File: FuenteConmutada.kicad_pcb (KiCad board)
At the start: 2 copper layers, 50 x 50 mm, 25 parts, among them J1 Conn_01x02_Socket, J2 Conn_01x03_Socket, U1 MT3608

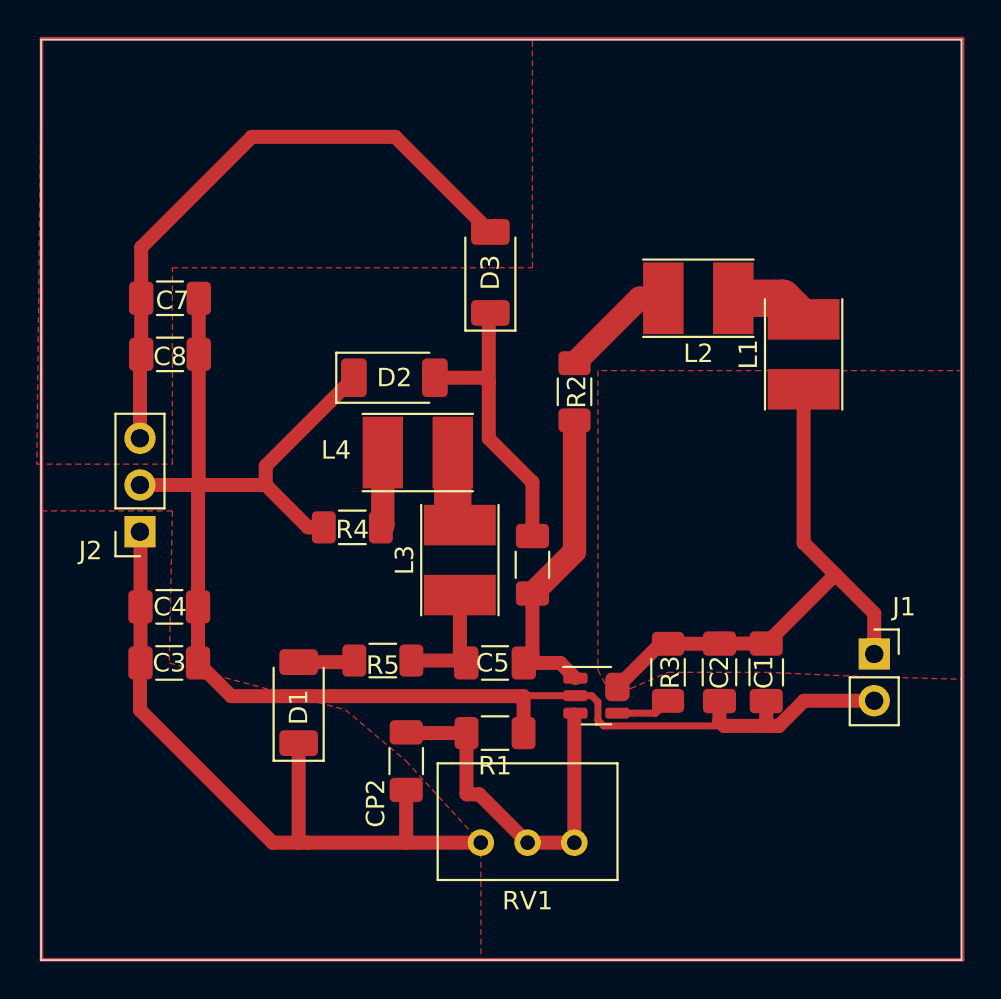
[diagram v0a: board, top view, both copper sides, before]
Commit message: Ajustes planos y tracks
Agrandar Margen a 40mils de los planos
Cambiar Rmed de lado del inductor (hacia Vin)
Cambiar Pos Inductores, mas cerca de SW
Aumentar a 50mils todos los tracks que no esten embutidos en planos
Puente en GND/Vfedback para no pasar debajo del SOT23
-Verificar cambios y poner Listo en la wiki
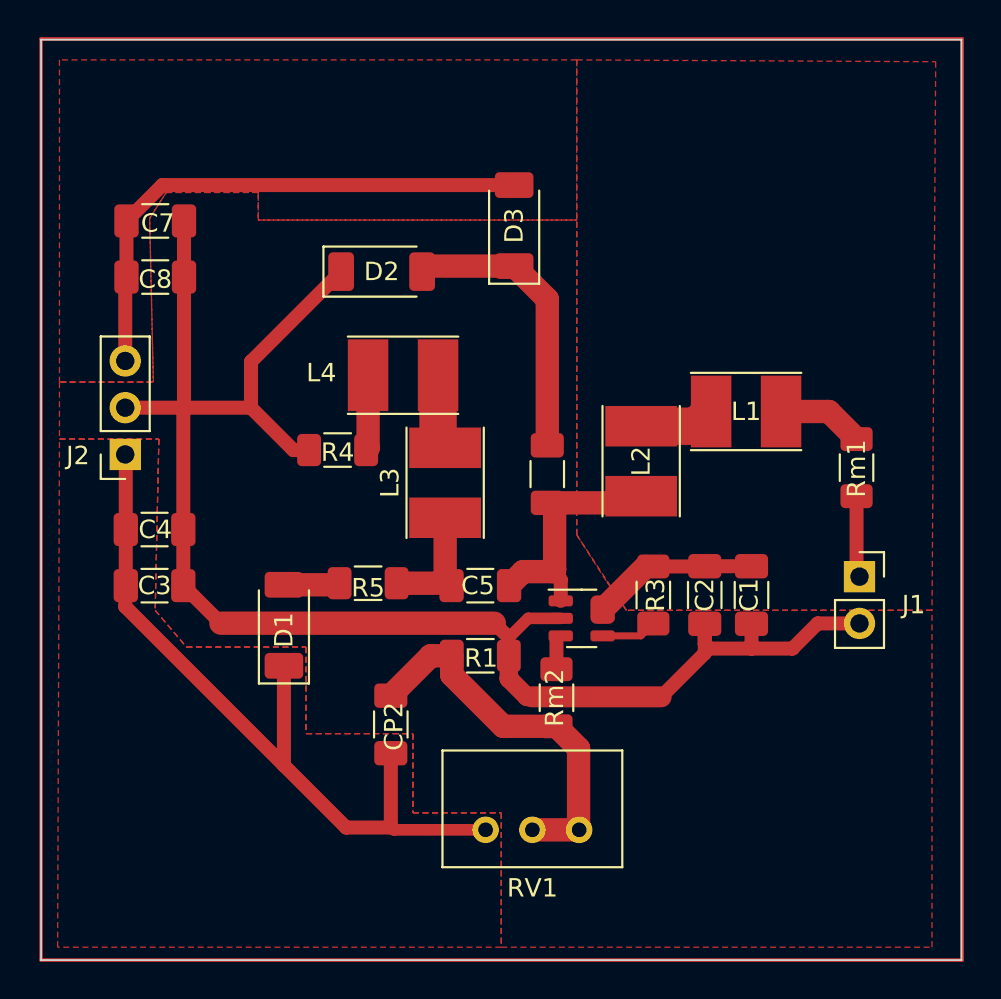
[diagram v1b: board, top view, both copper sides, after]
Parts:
- removed R2: R, Resistor_SMD:R_1206_3216Metric_Pad1.30x1.75mm_HandSolder
- added Rm1: R, Resistor_SMD:R_1206_3216Metric_Pad1.30x1.75mm_HandSolder, F.Cu at (109.3, 99.2)
- added Rm2: R, Resistor_SMD:R_1206_3216Metric_Pad1.30x1.75mm_HandSolder, F.Cu at (93.0, 111.8)
- moved L2 9.38 mm to (97.6, 98.9), turned to -90 degrees
- moved D2 5.81 mm to (83.5, 88.6)
- moved CP1 4.99 mm to (92.5, 99.6)
- moved L1 4.41 mm to (103.3, 96.2), turned to 180 degrees
- moved C3 4.28 mm to (71.2, 105.7)
- moved C4 4.28 mm to (71.2, 102.6)
- moved C5 4.28 mm to (88.9, 105.7)
- moved C7 4.28 mm to (71.2, 85.8)
- moved C8 4.28 mm to (71.2, 88.9)
- moved J2 4.28 mm to (69.6, 98.5)
- moved R1 4.28 mm to (88.9, 109.5)
- moved D1 4.28 mm to (78.2, 107.8)
- moved J1 4.28 mm to (109.5, 105.2)
- moved L3 4.28 mm to (87.0, 100.1)
- moved L4 4.28 mm to (84.7, 94.2)
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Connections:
- CP2 pad 1: Net-(U1-FB) -> Net-(CP2-Pad1)
- L1 pad 1: /Vin -> Net-(L1-Pad1)
- L2 pad 2: Net-(L2-Pad2) -> Net-(U1-SW)
- R1 pad 1: Net-(U1-FB) -> Net-(CP2-Pad1)
- RV1 pad 2: Net-(U1-FB) -> Net-(CP2-Pad1)
- RV1 pad 3: Net-(U1-FB) -> Net-(CP2-Pad1)
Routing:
- net Net-(CP2-Pad1): track 0.00 -> 20.8 mm
- net Net-(U1-FB): track 20.6 -> 2.23 mm
- net /Vin: track 30.8 -> 14.0 mm
- net GND: track 82.8 -> 89.8 mm
- net Net-(L2-Pad2): track 6.29 -> 0.00 mm
- net Net-(L1-Pad1): track 0.00 -> 4.72 mm
- net /Vo-: track 34.0 -> 29.5 mm
- net Net-(U1-SW): track 17.5 -> 13.7 mm
- net /Vo+: track 39.5 -> 42.4 mm

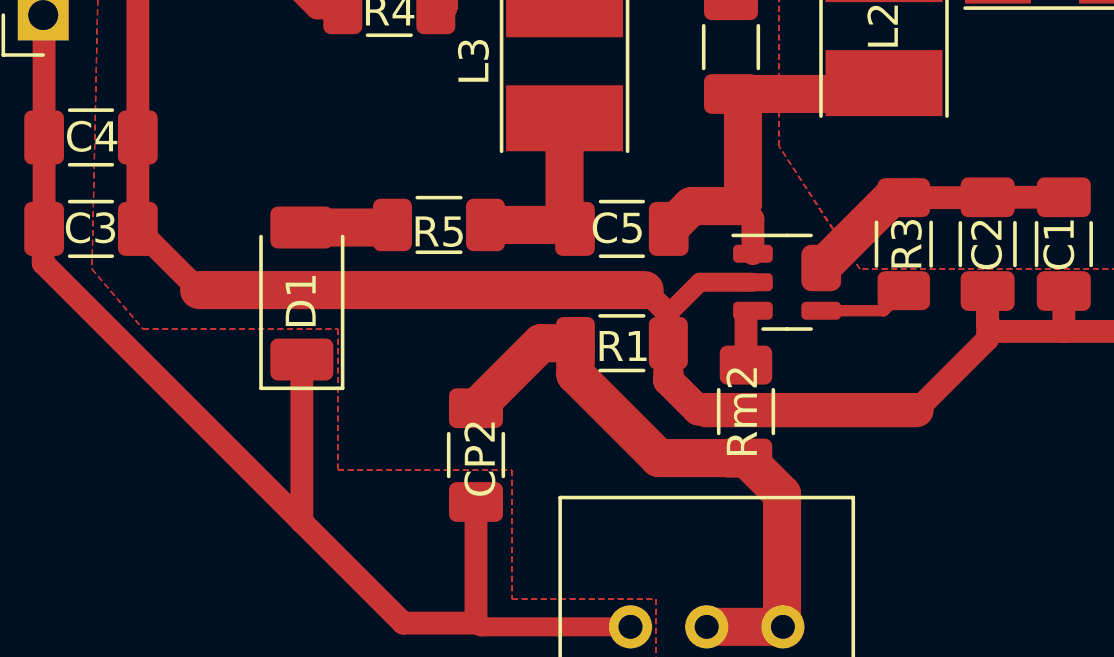
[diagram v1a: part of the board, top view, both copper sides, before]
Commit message: Acomodo de R1
Movi ligeramente R1 para aumentar la distancia a la pista GND
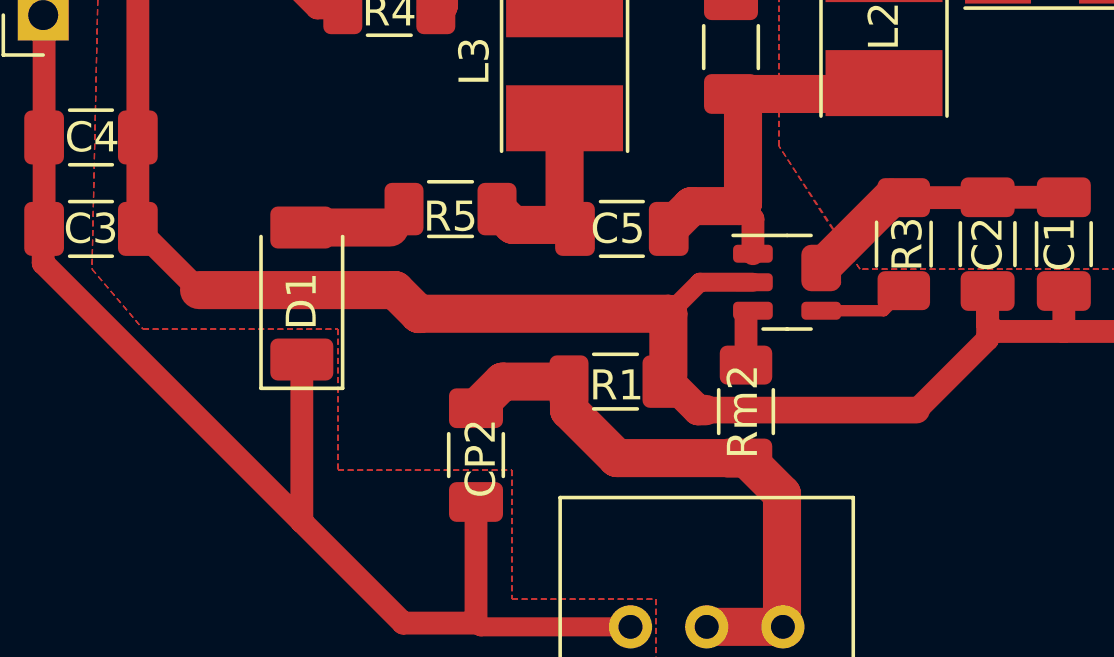
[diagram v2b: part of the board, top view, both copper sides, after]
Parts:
- moved R1 1.30 mm to (88.7, 110.8)
- moved R5 0.65 mm to (83.2, 105.0)
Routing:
- net Net-(CP2-Pad1): track 20.8 -> 19.7 mm
- net Net-(D1-A): track 3.06 -> 3.74 mm
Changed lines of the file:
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@@
   )
   (footprint "Resistor_SMD:R_1206_3216Metric_Pad1.30x1.75mm_HandSolder" (layer "F.Cu")
-    (at 88.862 109.47)
+    (at 88.65 110.75)
     (descr "Resistor SMD 1206 (3216 Metric), square (rectangular) end terminal, IPC_7351 nominal with elongated pad for handsoldering. (Body size source: IPC-SM-782 page 72, https://www.pcb-3d.com/wordpress/wp-content/uploads/ipc-sm-782a_amendment_1_and_2.pdf), generated with kicad-footprint-generator")
     (tags "resistor handsolder")
@@
   )
   (footprint "Resistor_SMD:R_1206_3216Metric_Pad1.30x1.75mm_HandSolder" (layer "F.Cu")
-    (at 82.766 105.528 180)
+    (at 83.15 105 180)
     (descr "Resistor SMD 1206 (3216 Metric), square (rectangular) end terminal, IPC_7351 nominal with elongated pad for handsoldering. (Body size source: IPC-SM-782 page 72, https://www.pcb-3d.com/wordpress/wp-content/uploads/ipc-sm-782a_amendment_1_and_2.pdf), generated with kicad-footprint-generator")
     (tags "resistor handsolder")
@@
   (segment (start 103.594 109.0785) (end 101.308 109.0785) (width 0.762) (layer "F.Cu") (net 1))
   (segment (start 103.594 107.7305) (end 103.594 109.0785) (width 0.762) (layer "F.Cu") (net 1))
-  (segment (start 74.768 107.7) (end 89.624 107.7) (width 1.27) (layer "F.Cu") (net 1))
+  (segment (start 82.112 108.488) (end 90.412 108.488) (width 1.27) (layer "F.Cu") (net 1))
   (segment (start 109.461 107.712) (end 107.188 107.712) (width 0.762) (layer "F.Cu") (net 1))
   (segment (start 72.7665 88.896) (end 72.7665 95.8995) (width 0.762) (layer "F.Cu") (net 1))
-  (segment (start 91.661789 111.7) (end 98.6865 111.7) (width 1.143) (layer "F.Cu") (net 1))
+  (segment (start 91.661789 111.7) (end 98.6865 111.7) (width 0.889) (layer "F.Cu") (net 1))
+  (segment (start 81.3 107.7) (end 82.1 108.5) (width 1.27) (layer "F.Cu") (net 1))
   (segment (start 101.054 107.7305) (end 101.054 108.8245) (width 0.762) (layer "F.Cu") (net 1))
   (segment (start 72.86 95.993) (end 69.573 95.993) (width 0.762) (layer "F.Cu") (net 1))
@@
   (segment (start 101.054 108.8245) (end 101.308 109.0785) (width 0.762) (layer "F.Cu") (net 1))
   (segment (start 76.405 93.495) (end 81.3 88.6) (width 0.762) (layer "F.Cu") (net 1))
-  (segment (start 90.412 108.488) (end 90.412 109.47) (width 0.635) (layer "F.Cu") (net 1))
+  (segment (start 90.412 110.538) (end 90.412 110.450211) (width 0.762) (layer "F.Cu") (net 1))
+  (segment (start 74.768 107.7) (end 81.3 107.7) (width 1.27) (layer "F.Cu") (net 1))
   (segment (start 91.4 111.7) (end 91.661789 111.7) (width 1.016) (layer "F.Cu") (net 1))
   (segment (start 105.8215 109.0785) (end 103.594 109.0785) (width 0.762) (layer "F.Cu") (net 1))
   (segment (start 76.405 95.993) (end 76.405 93.495) (width 0.762) (layer "F.Cu") (net 1))
   (segment (start 90.412 110.450211) (end 90.412 110.712) (width 1.016) (layer "F.Cu") (net 1))
-  (segment (start 89.624 107.7) (end 90.412 108.488) (width 0.762) (layer "F.Cu") (net 1))
+  (segment (start 90.412 110.538) (end 90.2 110.75) (width 0.635) (layer "F.Cu") (net 1))
+  (segment (start 90.412 108.488) (end 90.412 110.538) (width 1.27) (layer "F.Cu") (net 1))
   (segment (start 72.7665 85.848) (end 72.7665 88.896) (width 0.762) (layer "F.Cu") (net 1))
   (segment (start 79.56 98.294) (end 78.706 98.294) (width 0.762) (layer "F.Cu") (net 1))
@@
   (segment (start 107.188 107.712) (end 105.8215 109.0785) (width 0.762) (layer "F.Cu") (net 1))
   (segment (start 93.231 107.438) (end 91.462 107.438) (width 0.635) (layer "F.Cu") (net 1))
+  (segment (start 82.1 108.5) (end 82.112 108.488) (width 1.27) (layer "F.Cu") (net 1))
   (segment (start 91.462 107.438) (end 90.412 108.488) (width 0.635) (layer "F.Cu") (net 1))
   (segment (start 72.728 96.125) (end 72.86 95.993) (width 0.762) (layer "F.Cu") (net 1))
-  (segment (start 90.412 109.47) (end 90.412 110.450211) (width 0.762) (layer "F.Cu") (net 1))
   (segment (start 76.405 95.993) (end 72.86 95.993) (width 0.762) (layer "F.Cu") (net 1))
   (segment (start 72.728 105.66) (end 74.768 107.7) (width 0.762) (layer "F.Cu") (net 1))
   (segment (start 98.26 107.718) (end 97.59 108.388) (width 0.381) (layer "F.Cu") (net 2))
   (segment (start 97.59 108.388) (end 95.506 108.388) (width 0.381) (layer "F.Cu") (net 2))
-  (segment (start 81.13 105.614) (end 81.216 105.528) (width 0.762) (layer "F.Cu") (net 3))
+  (segment (start 81.6 105.144) (end 81.6 105) (width 0.762) (layer "F.Cu") (net 3))
+  (segment (start 81.13 105.614) (end 81.6 105.144) (width 0.762) (layer "F.Cu") (net 3))
   (segment (start 78.194 105.614) (end 81.13 105.614) (width 1.27) (layer "F.Cu") (net 3))
   (segment (start 109.3 105.011) (end 109.461 105.172) (width 1.27) (layer "F.Cu") (net 4))
@@
   (segment (start 82.766 98.188) (end 82.66 98.294) (width 1.27) (layer "F.Cu") (net 12))
   (segment (start 86.952 101.972) (end 86.952 105.3125) (width 1.27) (layer "F.Cu") (net 13))
+  (segment (start 85.228 105.528) (end 87.1675 105.528) (width 1.27) (layer "F.Cu") (net 13))
   (segment (start 87.2995 105.66) (end 87.2135 105.746) (width 0.762) (layer "F.Cu") (net 13))
+  (segment (start 84.7 105) (end 85.228 105.528) (width 1.27) (layer "F.Cu") (net 13))
   (segment (start 87.1675 105.528) (end 87.2995 105.66) (width 0.762) (layer "F.Cu") (net 13))
-  (segment (start 84.316 105.528) (end 87.1675 105.528) (width 1.27) (layer "F.Cu") (net 13))
   (segment (start 86.952 105.3125) (end 87.2995 105.66) (width 0.762) (layer "F.Cu") (net 13))
   (segment (start 105.2 96.2) (end 107.8 96.2) (width 1.27) (layer "F.Cu") (net 14))
   (segment (start 107.8 96.2) (end 109.3 97.7) (width 1.27) (layer "F.Cu") (net 14))
   (segment (start 94.2 114.5) (end 94.2 118.895) (width 1.27) (layer "F.Cu") (net 15))
-  (segment (start 93 113.3) (end 90.1 113.3) (width 1.27) (layer "F.Cu") (net 15))
-  (segment (start 90.1 113.3) (end 87.312 110.512) (width 1.27) (layer "F.Cu") (net 15))
-  (segment (start 87.312 110.512) (end 87.312 109.47) (width 1.27) (layer "F.Cu") (net 15))
+  (segment (start 84.8875 110.75) (end 84 111.6375) (width 1.27) (layer "F.Cu") (net 15))
+  (segment (start 87.1 110.75) (end 84.8875 110.75) (width 1.27) (layer "F.Cu") (net 15))
+  (segment (start 93 113.3) (end 88.7 113.3) (width 1.27) (layer "F.Cu") (net 15))
   (segment (start 93 113.3) (end 94.2 114.5) (width 1.27) (layer "F.Cu") (net 15))
-  (segment (start 86.1675 109.47) (end 84 111.6375) (width 1.27) (layer "F.Cu") (net 15))
   (segment (start 94.2 118.895) (end 94.23 118.925) (width 1.27) (layer "F.Cu") (net 15))
-  (segment (start 87.312 109.47) (end 86.1675 109.47) (width 1.27) (layer "F.Cu") (net 15))
+  (segment (start 87.1 111.7) (end 87.1 110.75) (width 1.27) (layer "F.Cu") (net 15))
+  (segment (start 88.7 113.3) (end 87.1 111.7) (width 1.27) (layer "F.Cu") (net 15))
   (segment (start 91.69 118.925) (end 94.23 118.925) (width 1.27) (layer "F.Cu") (net 15))
   (zone (net 4) (net_name "/Vin") (layer "F.Cu") (hatch edge 0.5)
